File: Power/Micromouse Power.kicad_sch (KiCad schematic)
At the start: 55 parts, among them J1 Battery, J2 Conn_02x08_Odd_Even, Q1 AO3401A, Q2 AO3401A, SW1 pwr, SW2 pwr, U1 AMS1117-3.3, U2 TP4056, U3 DRV8837, U4 DRV8837

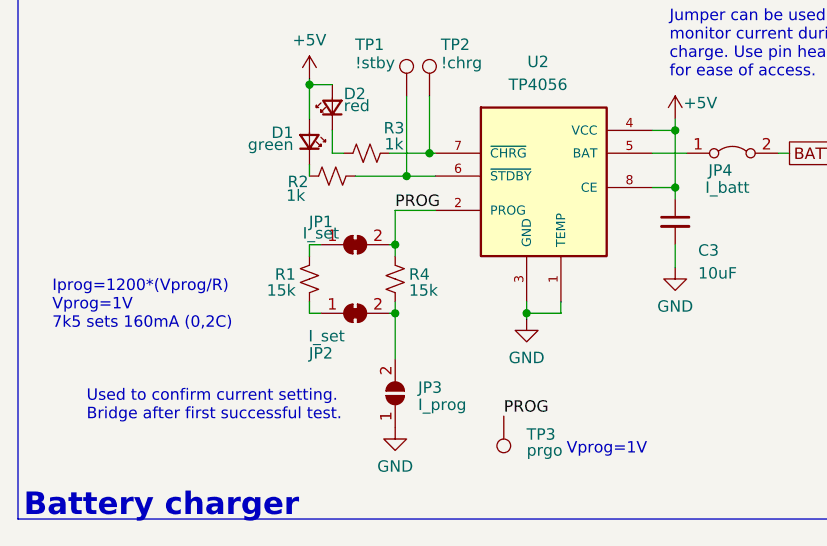
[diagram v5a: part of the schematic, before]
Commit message: Updated text on schematic
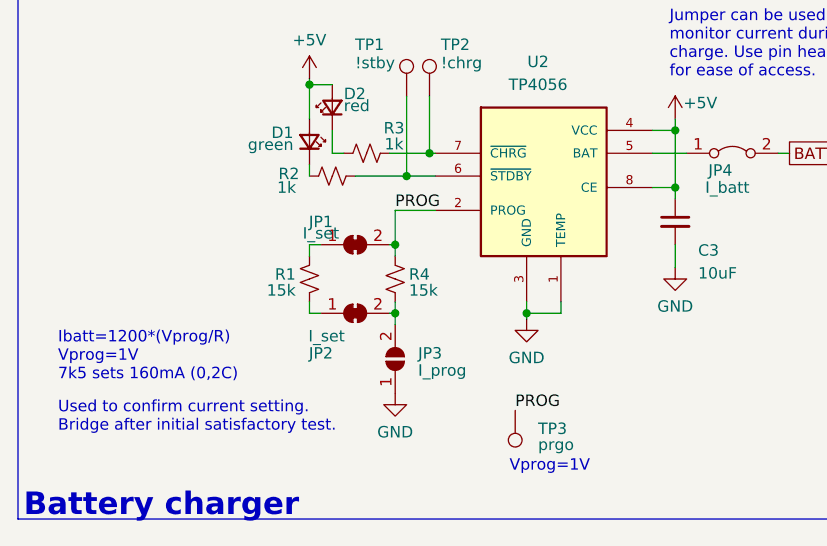
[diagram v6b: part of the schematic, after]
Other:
- note added: "Ibatt=1200*(Vprog/R) Vprog=1V 7k5 sets 160mA (0,2C)"
- note added: "Used to confirm current setting. Bridge after initial satisfactory test."
- note removed: "Iprog=1200*(Vprog/R) Vprog=1V 7k5 sets 160mA (0,2C)"
- note removed: "Used to confirm current setting. Bridge after first successful test."
- moved on the sheet: JP3, TP3
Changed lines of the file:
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@@
     (stroke (width 0) (type default))
   )
-  (wire (pts (xy 100.33 133.35) (xy 100.33 138.43))
+  (wire (pts (xy 100.33 133.35) (xy 100.33 134.62))
     (stroke (width 0) (type default))
   )
@@
     (effects (font (size 1.27 1.27)) (justify left bottom))
   )
-  (text "Vprog=1V" (at 119.38 149.225 0)
+  (text "Vprog=1V" (at 113.03 151.13 0)
     (effects (font (size 1.27 1.27)) (justify left bottom))
   )
@@
     (effects (font (size 1.27 1.27)) (justify left bottom))
   )
-  (text "Used to confirm current setting.\nBridge after first successful test."
-    (at 66.04 145.415 0)
+  (text "Used to confirm current setting.\nBridge after initial satisfactory test."
+    (at 62.865 146.685 0)
     (effects (font (size 1.27 1.27)) (justify left bottom))
   )
@@
     (effects (font (face "Arial") (size 2.5 2.5) (thickness 0.254) bold) (justify left bottom))
   )
-  (text "Iprog=1200*(Vprog/R)\nVprog=1V\n7k5 sets 160mA (0,2C)"
-    (at 62.23 135.255 0)
+  (text "Ibatt=1200*(Vprog/R)\nVprog=1V\n7k5 sets 160mA (0,2C)"
+    (at 62.865 140.97 0)
     (effects (font (size 1.27 1.27)) (justify left bottom))
   )
@@
     (effects (font (size 1.27 1.27)) (justify right bottom))
   )
-  (label "PROG" (at 112.395 144.78 0) (fields_autoplaced)
+  (label "PROG" (at 113.665 144.145 0) (fields_autoplaced)
     (effects (font (size 1.27 1.27)) (justify left bottom))
   )
@@
     )
   )
-  (symbol (lib_id "Connector:TestPoint") (at 112.395 144.78 180) (unit 1)
-    (in_bom yes) (on_board yes) (dnp no)
-    (property "Reference" "TP3" (at 114.935 146.812 0)
+  (symbol (lib_id "Connector:TestPoint") (at 113.665 144.145 180) (unit 1)
+    (in_bom yes) (on_board yes) (dnp no)
+    (property "Reference" "TP3" (at 116.205 146.177 0)
       (effects (font (size 1.27 1.27)) (justify right))
     )
-    (property "Value" "prgo" (at 114.935 148.59 0)
+    (property "Value" "prgo" (at 116.205 147.955 0)
       (effects (font (size 1.27 1.27)) (justify right))
     )
-    (property "Footprint" "TestPoint:TestPoint_Pad_D1.0mm" (at 107.315 144.78 0)
-      (effects (font (size 1.27 1.27)) hide)
-    )
-    (property "Datasheet" "~" (at 107.315 144.78 0)
+    (property "Footprint" "TestPoint:TestPoint_Pad_D1.0mm" (at 108.585 144.145 0)
+      (effects (font (size 1.27 1.27)) hide)
+    )
+    (property "Datasheet" "~" (at 108.585 144.145 0)
       (effects (font (size 1.27 1.27)) hide)
     )
@@
     )
   )
-  (symbol (lib_id "Jumper:SolderJumper_2_Open") (at 100.33 142.24 90) (unit 1)
-    (in_bom yes) (on_board yes) (dnp no)
-    (property "Reference" "JP3" (at 102.87 141.605 90)
+  (symbol (lib_id "Jumper:SolderJumper_2_Open") (at 100.33 138.43 90) (unit 1)
+    (in_bom yes) (on_board yes) (dnp no)
+    (property "Reference" "JP3" (at 102.87 137.795 90)
       (effects (font (size 1.27 1.27)) (justify right))
     )
-    (property "Value" "I_prog" (at 102.87 143.51 90)
+    (property "Value" "I_prog" (at 102.87 139.7 90)
       (effects (font (size 1.27 1.27)) (justify right))
     )
-    (property "Footprint" "Jumper:SolderJumper-2_P1.3mm_Open_RoundedPad1.0x1.5mm" (at 100.33 142.24 0)
-      (effects (font (size 1.27 1.27)) hide)
-    )
-    (property "Datasheet" "~" (at 100.33 142.24 0)
+    (property "Footprint" "Jumper:SolderJumper-2_P1.3mm_Open_RoundedPad1.0x1.5mm" (at 100.33 138.43 0)
+      (effects (font (size 1.27 1.27)) hide)
+    )
+    (property "Datasheet" "~" (at 100.33 138.43 0)
       (effects (font (size 1.27 1.27)) hide)
     )
@@
     )
   )
-  (symbol (lib_id "power:GND") (at 100.33 146.05 0) (unit 1)
+  (symbol (lib_id "power:GND") (at 100.33 142.24 0) (unit 1)
     (in_bom yes) (on_board yes) (dnp no) (fields_autoplaced)
-    (property "Reference" "#PWR07" (at 100.33 152.4 0)
-      (effects (font (size 1.27 1.27)) hide)
-    )
-    (property "Value" "GND" (at 100.33 150.368 0)
-      (effects (font (size 1.27 1.27)))
-    )
-    (property "Footprint" "" (at 100.33 146.05 0)
-      (effects (font (size 1.27 1.27)) hide)
-    )
-    (property "Datasheet" "" (at 100.33 146.05 0)
+    (property "Reference" "#PWR07" (at 100.33 148.59 0)
+      (effects (font (size 1.27 1.27)) hide)
+    )
+    (property "Value" "GND" (at 100.33 146.558 0)
+      (effects (font (size 1.27 1.27)))
+    )
+    (property "Footprint" "" (at 100.33 142.24 0)
+      (effects (font (size 1.27 1.27)) hide)
+    )
+    (property "Datasheet" "" (at 100.33 142.24 0)
       (effects (font (size 1.27 1.27)) hide)
     )
@@
   (symbol (lib_id "Device:R_Small_US") (at 93.345 118.11 90) (unit 1)
     (in_bom yes) (on_board yes) (dnp no)
-    (property "Reference" "R2" (at 89.535 118.745 90)
-      (effects (font (size 1.27 1.27)))
-    )
-    (property "Value" "1k" (at 89.281 120.269 90)
-      (effects (font (size 1.27 1.27)))
-    )
+    (property "Reference" "R2" (at 88.519 117.856 90)
+      (effects (font (size 1.27 1.27)))
+    )
+    (property "Value" "1k" (at 88.265 119.38 90)
+      (effects (font (size 1.27 1.27)))
+    )
